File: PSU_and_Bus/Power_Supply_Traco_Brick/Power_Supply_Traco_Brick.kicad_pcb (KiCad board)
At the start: 2 copper layers, 27.6 x 100 mm, 15 parts, among them J1 Conn_01x04, J2 USB_C_Receptacle, J3 Conn_01x02, U1 CH224K, U2 TEN10-2421WIN

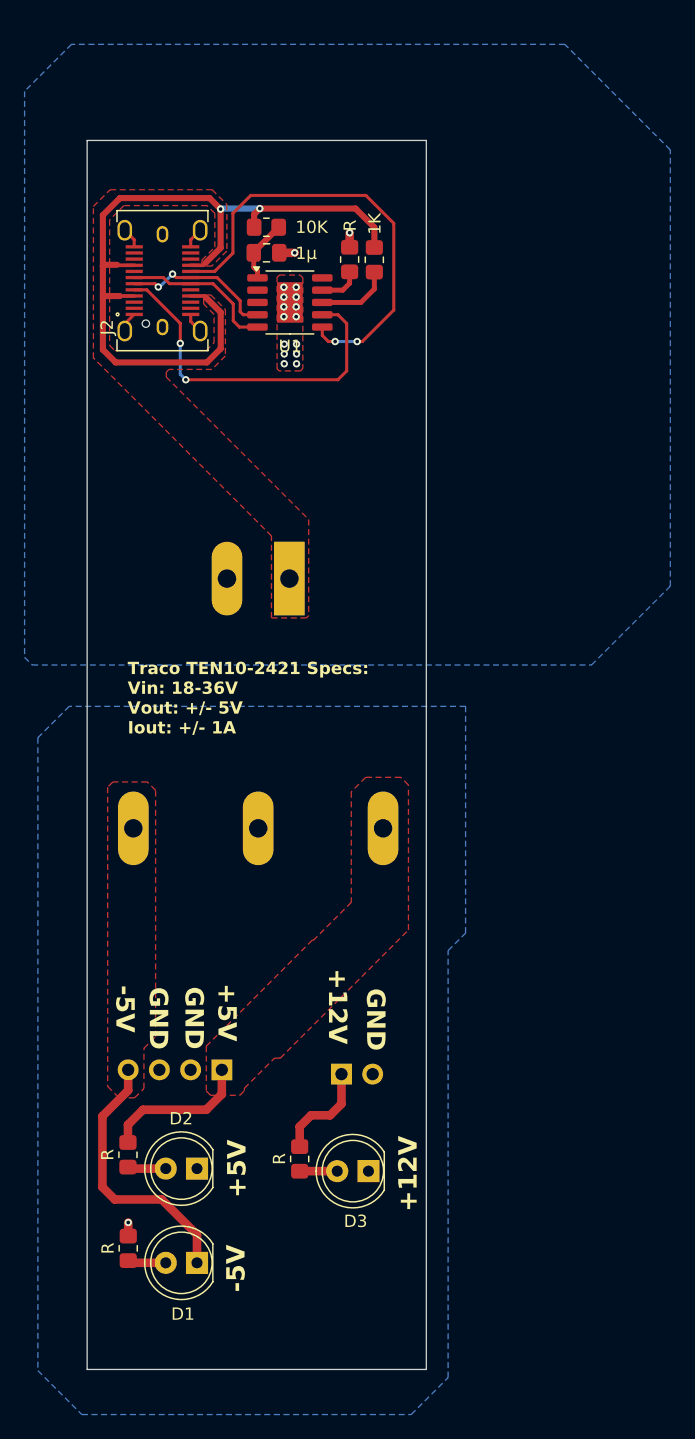
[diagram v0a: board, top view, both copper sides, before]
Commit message: fixed errors on PCB after DRC
- Traces too close to PCB edge
- overlap on F.Silkscreen
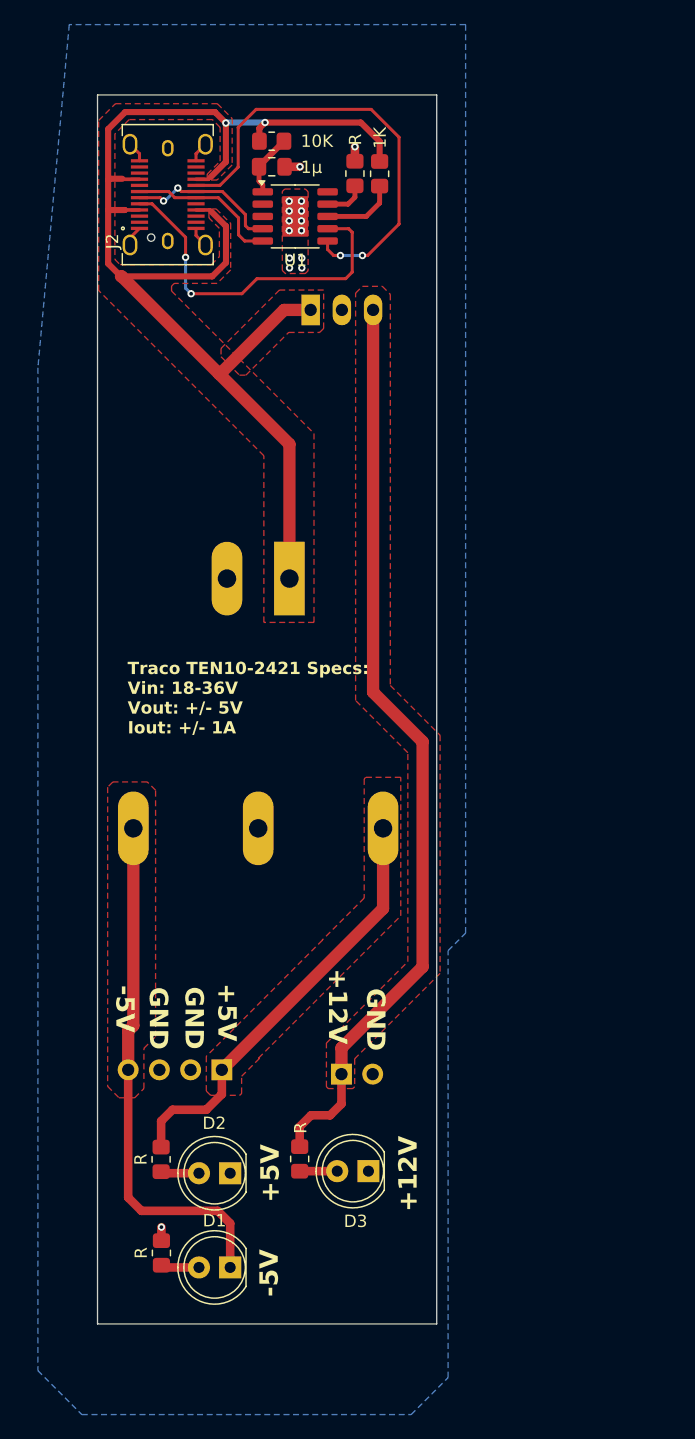
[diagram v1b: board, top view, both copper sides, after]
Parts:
- added U3: TSR_1-24120, Converter_DCDC:Converter_DCDC_TRACO_TSR-1_THT, B.Cu at (157.0, 68.5)
- moved R3 7.01 mm to (160.6, 57.4)
- moved C1 7.01 mm to (153.8, 56.8)
- moved R1 7.01 mm to (162.6, 57.4)
- moved R2 7.01 mm to (153.8, 54.7)
- moved U1 7.01 mm to (155.7, 60.9)
- moved J2 7.01 mm to (145.3, 59.1)
- moved R5 2.73 mm to (144.8, 137.6)
- moved D1 2.73 mm to (150.4, 146.4)
- moved D2 2.73 mm to (150.4, 138.7)
- moved R4 2.73 mm to (144.8, 145.2)
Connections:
- C1 pad 1: GND1 -> GND
- J2 pad A1: GND1 -> GND
- J2 pad A12: GND1 -> GND
- J2 pad B1: GND1 -> GND
- J2 pad B12: GND1 -> GND
- J2 pad S1: GND1 -> GND
- R3 pad 2: GND1 -> GND
- U1 pad 11: GND1 -> GND
- U2 pad 2: GND1 -> GND
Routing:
- net +12V: track 8.22 -> 74.8 mm
- net VBUS: track 65.7 -> 105.7 mm
- net +5V: track 12.1 -> 35.0 mm
- net -5V: track 22.0 -> 43.0 mm
- net GND1: track 9.11 -> 0.00 mm, vias 16 -> 0
- net GND: track 1.10 -> 10.2 mm, vias 1 -> 15
- added copper zone on F.Cu, net +12V
- added copper zone on F.Cu, net GND
- removed copper zone on B.Cu, net GND1
- removed copper zone on F.Cu, net GND1
